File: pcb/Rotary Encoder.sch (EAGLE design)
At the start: 7 parts

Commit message: Mid-project updates
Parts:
- added MGT1, MGT2, MGT3, MGT4: BEAGLEBONEBLACK_MOUNTING_HOLE, BeagleBone_Black_Wireless:BEAGLEBONEBLACK_MOUNTING_HOLE
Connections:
- net GND: now also MGT1.P$1, MGT2.P$1, MGT3.P$1, MGT4.P$1
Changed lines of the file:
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@@
 <part name="U$1" library="diy-modules" deviceset="DISPLAY-OLED-128X32" device=""/>
 <part name="P+2" library="audio amplifier example" library_urn="urn:adsk.eagle:library:970892" deviceset="VCC" device=""/>
+<part name="MGT1" library="BeagleBone_Black_Wireless" library_urn="urn:adsk.eagle:library:6644236" deviceset="BEAGLEBONEBLACK_MOUNTING_HOLE" device="" package3d_urn="urn:adsk.eagle:package:6644362/2"/>
+<part name="MGT2" library="BeagleBone_Black_Wireless" library_urn="urn:adsk.eagle:library:6644236" deviceset="BEAGLEBONEBLACK_MOUNTING_HOLE" device="" package3d_urn="urn:adsk.eagle:package:6644362/2"/>
+<part name="MGT3" library="BeagleBone_Black_Wireless" library_urn="urn:adsk.eagle:library:6644236" deviceset="BEAGLEBONEBLACK_MOUNTING_HOLE" device="" package3d_urn="urn:adsk.eagle:package:6644362/2"/>
+<part name="MGT4" library="BeagleBone_Black_Wireless" library_urn="urn:adsk.eagle:library:6644236" deviceset="BEAGLEBONEBLACK_MOUNTING_HOLE" device="" package3d_urn="urn:adsk.eagle:package:6644362/2"/>
+<part name="SUPPLY5" library="supply2" library_urn="urn:adsk.eagle:library:372" deviceset="GND" device=""/>
 </parts>
 <sheets>
@@
 <attribute name="VALUE" x="72.136" y="85.344" size="1.27" layer="96" rot="R270"/>
 </instance>
+<instance part="MGT1" gate="G$1" x="20.32" y="172.72" smashed="yes">
+<attribute name="NAME" x="21.082" y="170.688" size="1.27" layer="95"/>
+</instance>
+<instance part="MGT2" gate="G$1" x="27.94" y="172.72" smashed="yes">
+<attribute name="NAME" x="28.702" y="170.688" size="1.27" layer="95"/>
+</instance>
+<instance part="MGT3" gate="G$1" x="35.56" y="172.72" smashed="yes">
+<attribute name="NAME" x="36.322" y="170.688" size="1.27" layer="95"/>
+</instance>
+<instance part="MGT4" gate="G$1" x="43.18" y="172.72" smashed="yes">
+<attribute name="NAME" x="43.942" y="170.688" size="1.27" layer="95"/>
+</instance>
+<instance part="SUPPLY5" gate="GND" x="43.18" y="160.02" smashed="yes">
+<attribute name="VALUE" x="41.275" y="156.845" size="1.778" layer="96"/>
+</instance>
 </instances>
 <busses>
@@
 <wire x1="170.18" y1="68.58" x2="170.18" y2="66.04" width="0.1524" layer="91"/>
 </segment>
+<segment>
+<pinref part="MGT1" gate="G$1" pin="P$1"/>
+<pinref part="SUPPLY5" gate="GND" pin="GND"/>
+<wire x1="20.32" y1="167.64" x2="27.94" y2="167.64" width="0.1524" layer="91"/>
+<wire x1="27.94" y1="167.64" x2="35.56" y2="167.64" width="0.1524" layer="91"/>
+<wire x1="35.56" y1="167.64" x2="43.18" y2="167.64" width="0.1524" layer="91"/>
+<wire x1="43.18" y1="167.64" x2="43.18" y2="162.56" width="0.1524" layer="91"/>
+<pinref part="MGT2" gate="G$1" pin="P$1"/>
+<junction x="27.94" y="167.64"/>
+<pinref part="MGT3" gate="G$1" pin="P$1"/>
+<junction x="35.56" y="167.64"/>
+<pinref part="MGT4" gate="G$1" pin="P$1"/>
+<junction x="43.18" y="167.64"/>
+</segment>
 </net>

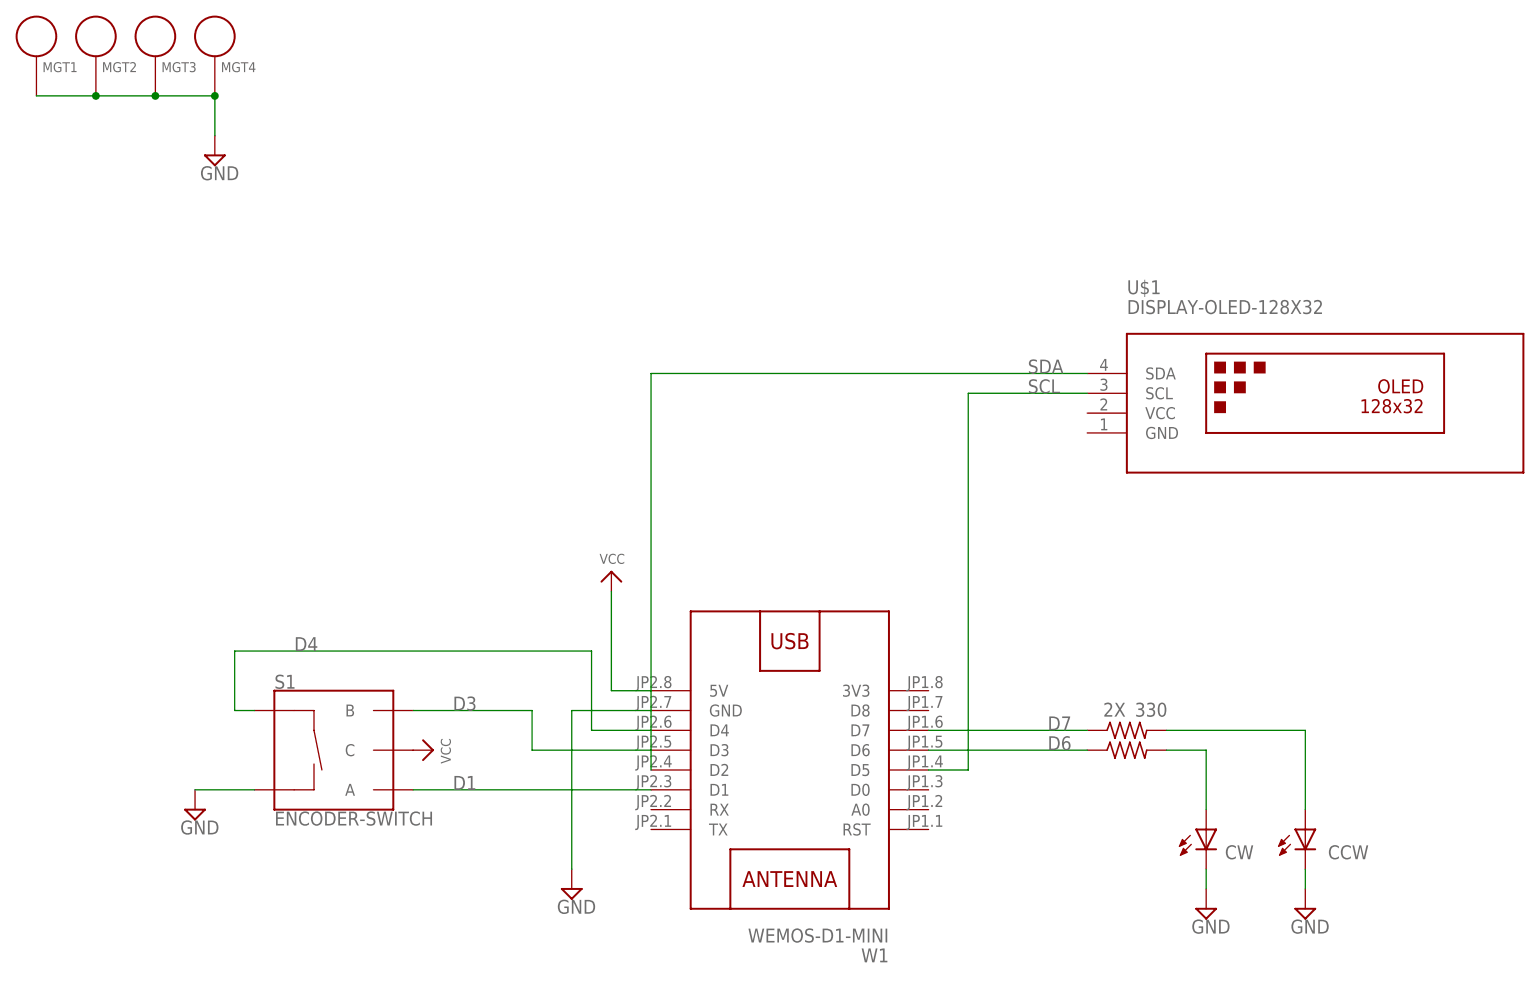
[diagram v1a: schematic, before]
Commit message: Reassign D1, D2
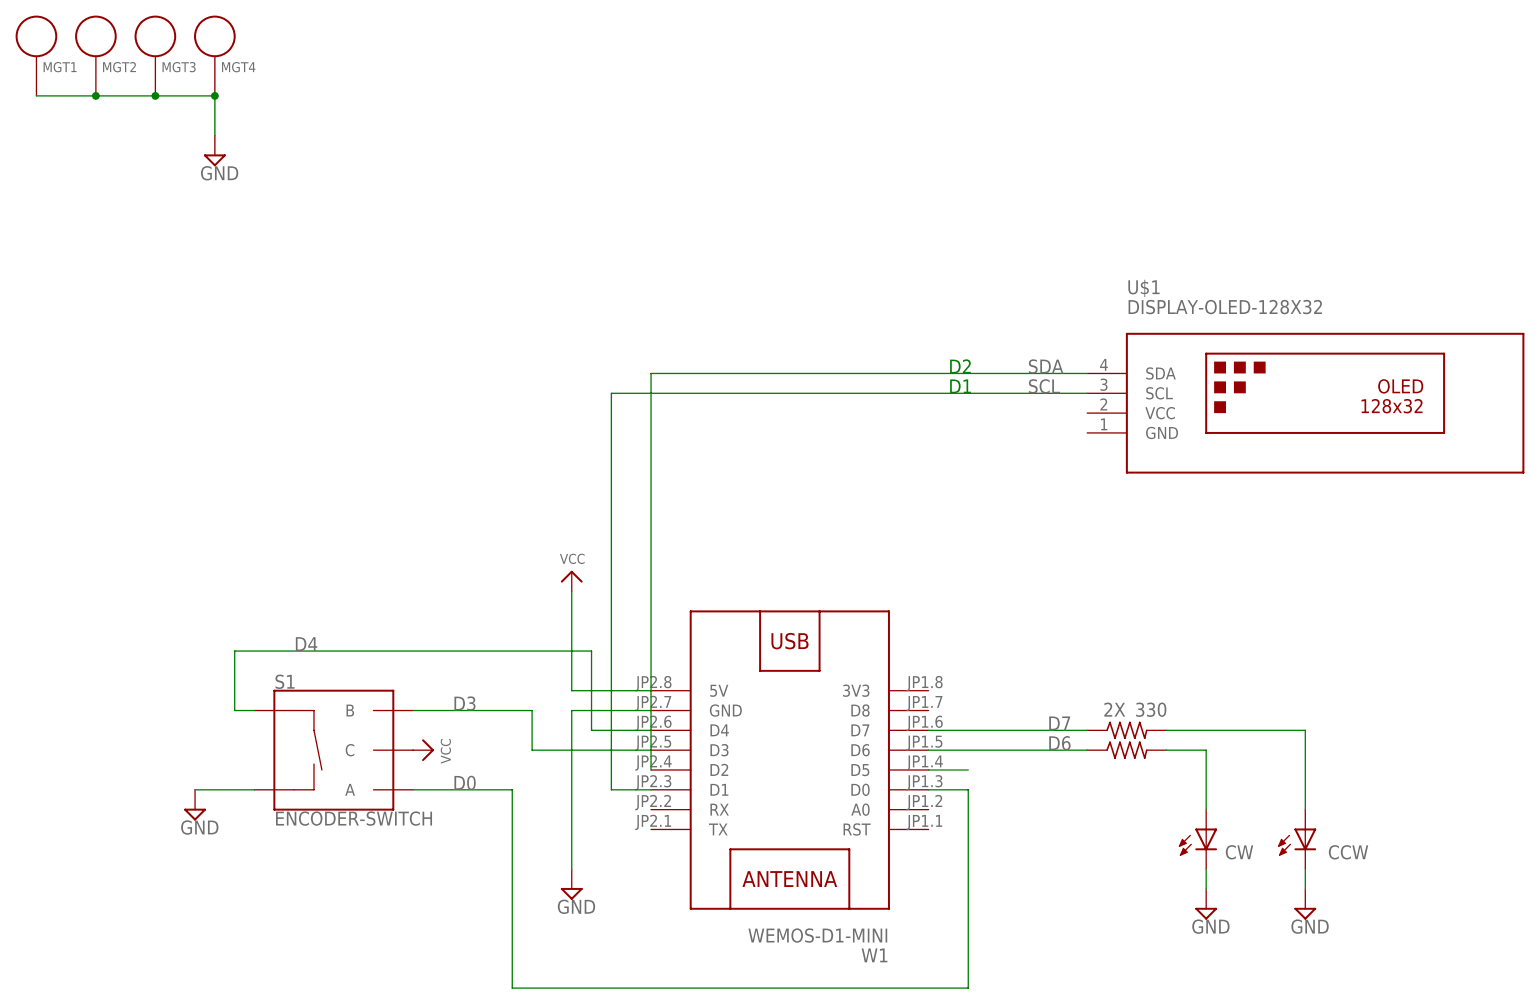
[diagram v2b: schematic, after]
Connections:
- new net D0: S1.A, W1.D0
- net D1: now also U$1.SCL; no longer S1.A
- net SCL: no longer U$1.SCL
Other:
- note added: "D1"
- note added: "D2"
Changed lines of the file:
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@@
 <sheet>
 <plain>
+<text x="137.16" y="132.08" size="1.778" layer="91">D2</text>
+<text x="137.16" y="129.54" size="1.778" layer="91">D1</text>
 </plain>
 <instances>
@@
 <attribute name="VALUE" x="180.975" y="60.325" size="1.778" layer="96"/>
 </instance>
-<instance part="P+1" gate="VCC" x="93.98" y="106.68" smashed="yes">
-<attribute name="VALUE" x="92.456" y="107.696" size="1.27" layer="96"/>
+<instance part="P+1" gate="VCC" x="88.9" y="106.68" smashed="yes">
+<attribute name="VALUE" x="87.376" y="107.696" size="1.27" layer="96"/>
 </instance>
 <instance part="FRAME1" gate="G$1" x="0" y="0" smashed="yes"/>
@@
 </busses>
 <nets>
-<net name="D1" class="0">
-<segment>
-<pinref part="S1" gate="G$1" pin="A"/>
-<pinref part="W1" gate="G$1" pin="D1"/>
-<wire x1="68.58" y1="78.74" x2="99.06" y2="78.74" width="0.1524" layer="91"/>
-<label x="73.66" y="78.74" size="1.778" layer="95"/>
-</segment>
-</net>
 <net name="GND" class="0">
 <segment>
@@
 <pinref part="P+1" gate="VCC" pin="VCC"/>
 <pinref part="W1" gate="G$1" pin="5V"/>
-<wire x1="93.98" y1="91.44" x2="93.98" y2="104.14" width="0.1524" layer="91"/>
-<wire x1="99.06" y1="91.44" x2="93.98" y2="91.44" width="0.1524" layer="91"/>
+<wire x1="88.9" y1="91.44" x2="88.9" y2="104.14" width="0.1524" layer="91"/>
+<wire x1="99.06" y1="91.44" x2="88.9" y2="91.44" width="0.1524" layer="91"/>
 </segment>
 <segment>
@@
 <pinref part="W1" gate="G$1" pin="D5"/>
 <wire x1="139.7" y1="81.28" x2="134.62" y2="81.28" width="0.1524" layer="91"/>
-<wire x1="139.7" y1="81.28" x2="139.7" y2="129.54" width="0.1524" layer="91"/>
-<pinref part="U$1" gate="G$1" pin="SCL"/>
-<wire x1="139.7" y1="129.54" x2="154.94" y2="129.54" width="0.1524" layer="91"/>
 <label x="147.32" y="129.54" size="1.778" layer="95"/>
 </segment>
@@
 <pinref part="W1" gate="G$1" pin="D2"/>
 <wire x1="99.06" y1="81.28" x2="99.06" y2="132.08" width="0.1524" layer="91"/>
+<label x="147.32" y="132.08" size="1.778" layer="95"/>
 <pinref part="U$1" gate="G$1" pin="SDA"/>
 <wire x1="99.06" y1="132.08" x2="154.94" y2="132.08" width="0.1524" layer="91"/>
-<label x="147.32" y="132.08" size="1.778" layer="95"/>
-</segment>
-</net>
+</segment>
+</net>
+<net name="D0" class="0">
+<segment>
+<pinref part="S1" gate="G$1" pin="A"/>
+<wire x1="68.58" y1="78.74" x2="81.28" y2="78.74" width="0.1524" layer="91"/>
+<wire x1="81.28" y1="78.74" x2="81.28" y2="53.34" width="0.1524" layer="91"/>
+<wire x1="81.28" y1="53.34" x2="139.7" y2="53.34" width="0.1524" layer="91"/>
+<wire x1="139.7" y1="53.34" x2="139.7" y2="78.74" width="0.1524" layer="91"/>
+<pinref part="W1" gate="G$1" pin="D0"/>
+<wire x1="139.7" y1="78.74" x2="134.62" y2="78.74" width="0.1524" layer="91"/>
+<label x="73.66" y="78.74" size="1.778" layer="95"/>
+</segment>
+</net>
+<net name="D1" class="0">
+<segment>
+<pinref part="W1" gate="G$1" pin="D1"/>
+<wire x1="99.06" y1="78.74" x2="93.98" y2="78.74" width="0.1524" layer="91"/>
+<wire x1="93.98" y1="78.74" x2="93.98" y2="129.54" width="0.1524" layer="91"/>
+<pinref part="U$1" gate="G$1" pin="SCL"/>
+<wire x1="93.98" y1="129.54" x2="154.94" y2="129.54" width="0.1524" layer="91"/>
+</segment>
+</net>
